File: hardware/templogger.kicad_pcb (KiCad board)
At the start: 2 copper layers, 50 x 70 mm, 53 parts, among them J101 Conn_K_TERM_XH_2P, J102 Conn_01x02, J103 USB_B_Mini, J104 LiPo BATTERY, J105 CPROBE, Q101 2N7002K, Q102 IRF7606PBF, SW101 SW_Push_LED, SW102 SW_Push_LED, SW103 BOOT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

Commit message: Add gerber file and update BOM list
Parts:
- removed J105: CPROBE, Connector_PinHeader_1.27mm:PinHeader_1x02_P1.27mm_Vertical
- removed R116: 0.1, tbctl:R_0805_2012Metric_Pad1.20x1.40mm_HandSolder
- removed REF** (x4): MountingHole_3.2mm_M3, MountingHole:MountingHole_3.2mm_M3
- added C111: 0.1uF, Capacitor_SMD:C_0603_1608Metric_Pad1.08x0.95mm_HandSolder, B.Cu at (91.1, 80.5)
- added JP101: SolderJumper_2_Open, Jumper:SolderJumper-2_P1.3mm_Open_RoundedPad1.0x1.5mm, F.Cu at (110.1, 60.7)
- added R117: 20K 1%, tbctl:R_0805_2012Metric_Pad1.20x1.40mm_HandSolder, F.Cu at (109.0, 57.4)
- added R118: 10K, tbctl:R_0805_2012Metric_Pad1.20x1.40mm_HandSolder, B.Cu at (91.2, 82.8)
- added SW105: SLIDE_SW, tbctl:SLIDE_SW_IS1235-G, F.Cu at (90.9, 57.0)
- J104: moved to F.Cu
- R108: value 10K -> 20K 1%
- moved R108 6.90 mm to (114.6, 57.4)
- moved J104 2.20 mm to (89.3, 66.6)
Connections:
- J103 pad 6: GND -> Net-(J103-Shield)
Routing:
- net Net-(J103-Shield): track 0.00 -> 20.2 mm
- net Net-(JP101-A): track 14.4 -> 23.4 mm
- net /GPIO2: track 5.14 -> 13.1 mm
- net Net-(JP101-B): track 28.2 -> 36.1 mm
- net +3.3V: track 136.4 -> 129.6 mm
- net GND: track 84.8 -> 89.2 mm
- net /VBAT: track 14.1 -> 16.3 mm
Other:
- board text added: "OFF"
- board text added: "TEMP-LOGGER 2023 (C) HNZ Rev.2"
- board text removed: "CT"
- board text removed: "TMP LOGGER 2023 (C) HNZ"

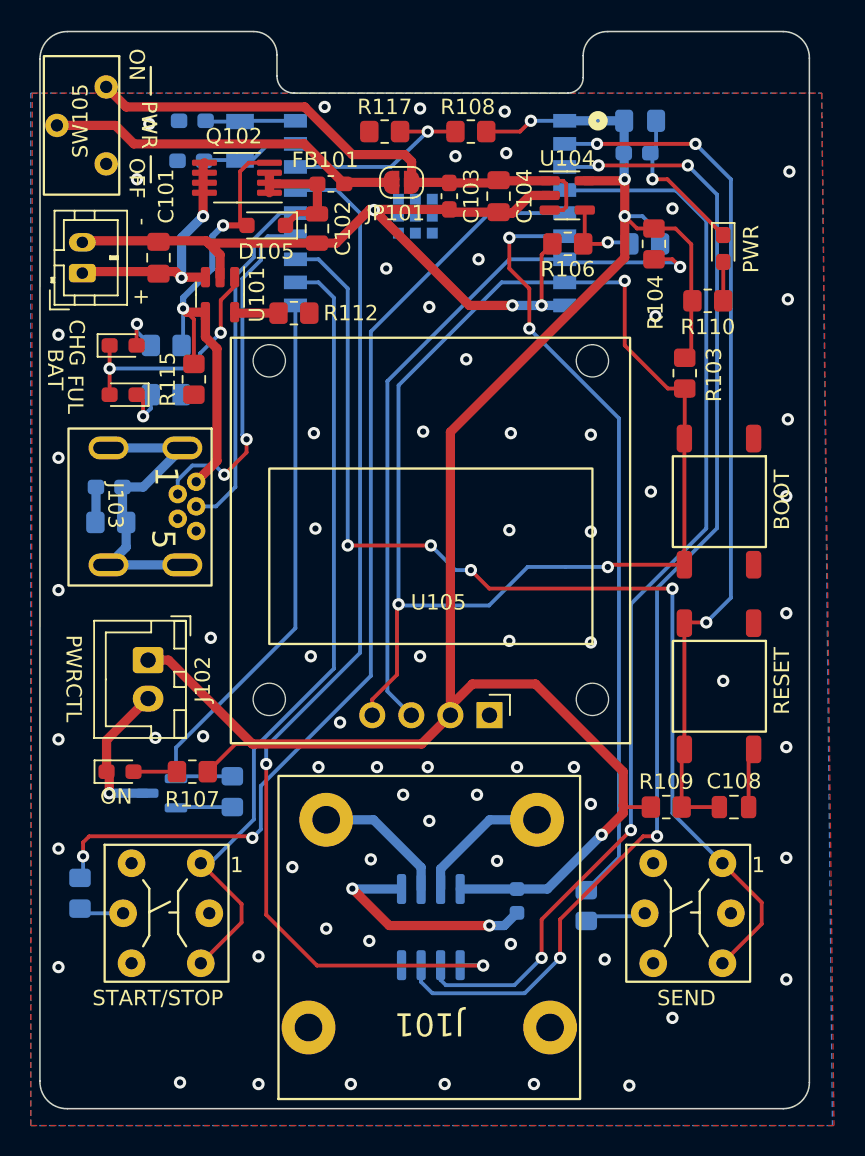
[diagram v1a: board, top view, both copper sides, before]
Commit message: Fixed battery socket
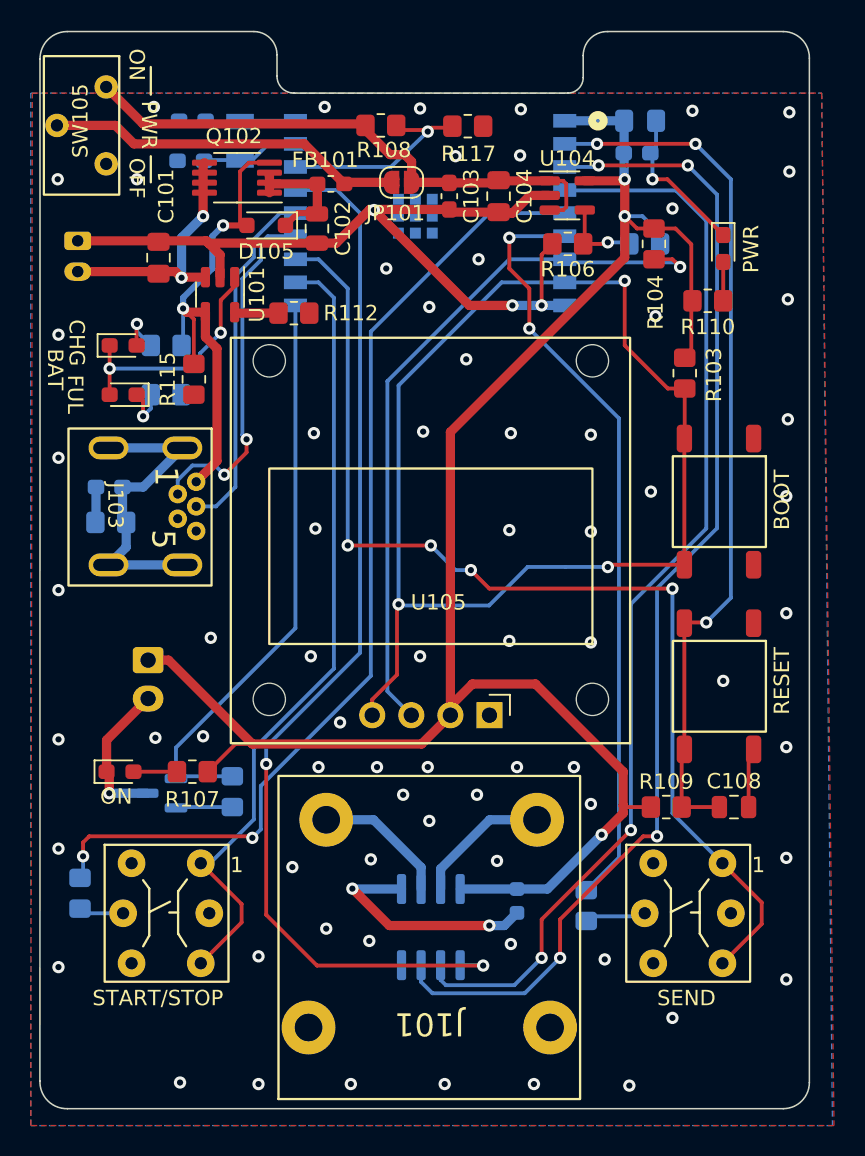
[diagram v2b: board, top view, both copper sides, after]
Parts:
- D101, D102, D103: value LED RED -> LED RED SML-E12V8WT86
- D104: value LED GREEN -> LED GREEN SML-E12P8WT86
- J102: moved to B.Cu
- J104: value LiPo BATTERY -> LiPo BATTERY Socket; moved to B.Cu
- Q102: value IRF7606PBF -> IRF7606TRPBF
- SW103: value BOOT -> BOOT TS-06104
- SW104: value RESET -> RESET TS-06104
- SW105: value SLIDE_SW -> SLIDE_SW IS-1245T-G
- moved R108 5.86 mm to (108.8, 57.0), turned to 0 degrees
- moved R117 5.41 mm to (114.4, 57.0), turned to 0 degrees
- moved J104 2.12 mm to (89.0, 64.5), turned to -90 degrees
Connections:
- C103 pad 1: Net-(JP101-B) -> /VIN
- C104 pad 1: Net-(JP101-B) -> /VIN
- J104 pad 1: /VBAT -> GND
- J104 pad 2: GND -> /VBAT
- JP101 pad 2: Net-(JP101-B) -> /VIN
- R108 pad 1: +3.3V -> /VIN
- SW105 pad 1: Net-(JP101-B) -> /VIN
- U104 pad 1: Net-(JP101-B) -> /VIN
- U104 pad 3: Net-(JP101-B) -> /VIN
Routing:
- net /VIN: track 0.00 -> 36.7 mm
- net Net-(JP101-B): track 36.1 -> 0.00 mm
- net +3.3V: track 129.6 -> 124.2 mm, vias 4 -> 3
- net GND: vias 74 -> 77
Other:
- board text added: "TEMP-LOGGER 2023 (C) HNZ Rev.4"
- board text removed: "TEMP-LOGGER 2023 (C) HNZ Rev.2"
